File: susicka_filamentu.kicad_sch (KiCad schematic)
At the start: 33 parts, among them J1 USB_C_Receptacle_USB2.0_16P, J2 Conn_01x03, J3 Conn_01x04, J5 SHT40_I2C, J6 HX711_Weight, J7 Heater_Output, Q1 AO3400A, U1 RP2350A-QFN60

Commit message: revert(pcb): restore original clean schematic file to prevent KiCad crash
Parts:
- removed J5: SHT40_I2C, Connector_PinHeader_2.54mm:PinHeader_1x04_P2.54mm_Vertical, symbol Connector_Generic:Conn_01x04
- removed J6: HX711_Weight, Connector_PinHeader_2.54mm:PinHeader_1x04_P2.54mm_Vertical, symbol Connector_Generic:Conn_01x04
- removed J7: Heater_Output, TerminalBlock_Phoenix:TerminalBlock_Phoenix_MKDS-1,5-2_1x02_P5.00mm_Horizontal, symbol Connector_Generic:Conn_01x02
- removed Q1: AO3400A, Package_TO_SOT_SMD:SOT-23, symbol Transistor_FET:Q_NMOS_GSD
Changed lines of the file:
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@@
 		)
 	)
-		(symbol
-		(lib_id "Connector_Generic:Conn_01x04")
-		(at 180.34 165.1 0)
-		(unit 1)
-		(exclude_from_sim no)
-		(in_bom yes)
-		(on_board yes)
-		(dnp no)
-		(fields_autoplaced yes)
-		(property "Reference" "J5"
-			(at 180.34 156.21 0)
-			(effects (font (size 1.27 1.27)))
-		)
-		(property "Value" "SHT40_I2C"
-			(at 180.34 158.75 0)
-			(effects (font (size 1.27 1.27)))
-		)
-		(property "Footprint" "Connector_PinHeader_2.54mm:PinHeader_1x04_P2.54mm_Vertical"
-			(at 180.34 165.1 0)
-			(effects (font (size 1.27 1.27)) (hide yes))
-		)
-		(property "Datasheet" "~"
-			(at 180.34 165.1 0)
-			(effects (font (size 1.27 1.27)) (hide yes))
-		)
-		(property "Description" "Generic connector 1x04 for SHT40 Temp/Humidity Sensor"
-			(at 180.34 165.1 0)
-			(effects (font (size 1.27 1.27)) (hide yes))
-		)
-		(pin "1")
-		(pin "2")
-		(pin "3")
-		(pin "4")
-		(instances
-			(project ""
-				(path "/202a5452-a4a8-46b1-91e1-aa7f241e9adc"
-					(reference "J5")
-					(unit 1)
-				)
-			)
-		)
-	)
-	(symbol
-		(lib_id "Connector_Generic:Conn_01x04")
-		(at 210.82 165.1 0)
-		(unit 1)
-		(exclude_from_sim no)
-		(in_bom yes)
-		(on_board yes)
-		(dnp no)
-		(fields_autoplaced yes)
-		(property "Reference" "J6"
-			(at 210.82 156.21 0)
-			(effects (font (size 1.27 1.27)))
-		)
-		(property "Value" "HX711_Weight"
-			(at 210.82 158.75 0)
-			(effects (font (size 1.27 1.27)))
-		)
-		(property "Footprint" "Connector_PinHeader_2.54mm:PinHeader_1x04_P2.54mm_Vertical"
-			(at 210.82 165.1 0)
-			(effects (font (size 1.27 1.27)) (hide yes))
-		)
-		(property "Datasheet" "~"
-			(at 210.82 165.1 0)
-			(effects (font (size 1.27 1.27)) (hide yes))
-		)
-		(property "Description" "Generic connector 1x04 for HX711 Load Cell Amplifier"
-			(at 210.82 165.1 0)
-			(effects (font (size 1.27 1.27)) (hide yes))
-		)
-		(pin "1")
-		(pin "2")
-		(pin "3")
-		(pin "4")
-		(instances
-			(project ""
-				(path "/202a5452-a4a8-46b1-91e1-aa7f241e9adc"
-					(reference "J6")
-					(unit 1)
-				)
-			)
-		)
-	)
-	(symbol
-		(lib_id "Transistor_FET:Q_NMOS_GSD")
-		(at 245.11 165.1 0)
-		(unit 1)
-		(exclude_from_sim no)
-		(in_bom yes)
-		(on_board yes)
-		(dnp no)
-		(fields_autoplaced yes)
-		(property "Reference" "Q1"
-			(at 245.11 156.21 0)
-			(effects (font (size 1.27 1.27)))
-		)
-		(property "Value" "AO3400A"
-			(at 245.11 158.75 0)
-			(effects (font (size 1.27 1.27)))
-		)
-		(property "Footprint" "Package_TO_SOT_SMD:SOT-23"
-			(at 245.11 165.1 0)
-			(effects (font (size 1.27 1.27)) (hide yes))
-		)
-		(property "Datasheet" "~"
-			(at 245.11 165.1 0)
-			(effects (font (size 1.27 1.27)) (hide yes))
-		)
-		(property "Description" "N-Channel MOSFET Heater Switch"
-			(at 245.11 165.1 0)
-			(effects (font (size 1.27 1.27)) (hide yes))
-		)
-		(pin "1")
-		(pin "2")
-		(pin "3")
-		(instances
-			(project ""
-				(path "/202a5452-a4a8-46b1-91e1-aa7f241e9adc"
-					(reference "Q1")
-					(unit 1)
-				)
-			)
-		)
-	)
-	(symbol
-		(lib_id "Connector_Generic:Conn_01x02")
-		(at 275.6 165.1 0)
-		(unit 1)
-		(exclude_from_sim no)
-		(in_bom yes)
-		(on_board yes)
-		(dnp no)
-		(fields_autoplaced yes)
-		(property "Reference" "J7"
-			(at 275.6 156.21 0)
-			(effects (font (size 1.27 1.27)))
-		)
-		(property "Value" "Heater_Output"
-			(at 275.6 158.75 0)
-			(effects (font (size 1.27 1.27)))
-		)
-		(property "Footprint" "TerminalBlock_Phoenix:TerminalBlock_Phoenix_MKDS-1,5-2_1x02_P5.00mm_Horizontal"
-			(at 275.6 165.1 0)
-			(effects (font (size 1.27 1.27)) (hide yes))
-		)
-		(property "Datasheet" "~"
-			(at 275.6 165.1 0)
-			(effects (font (size 1.27 1.27)) (hide yes))
-		)
-		(property "Description" "Heater Screw Terminal Output"
-			(at 275.6 165.1 0)
-			(effects (font (size 1.27 1.27)) (hide yes))
-		)
-		(pin "1")
-		(pin "2")
-		(instances
-			(project ""
-				(path "/202a5452-a4a8-46b1-91e1-aa7f241e9adc"
-					(reference "J7")
-					(unit 1)
-				)
-			)
-		)
-	)
-(sheet_instances
+	(sheet_instances
 		(path "/"
 			(page "1")

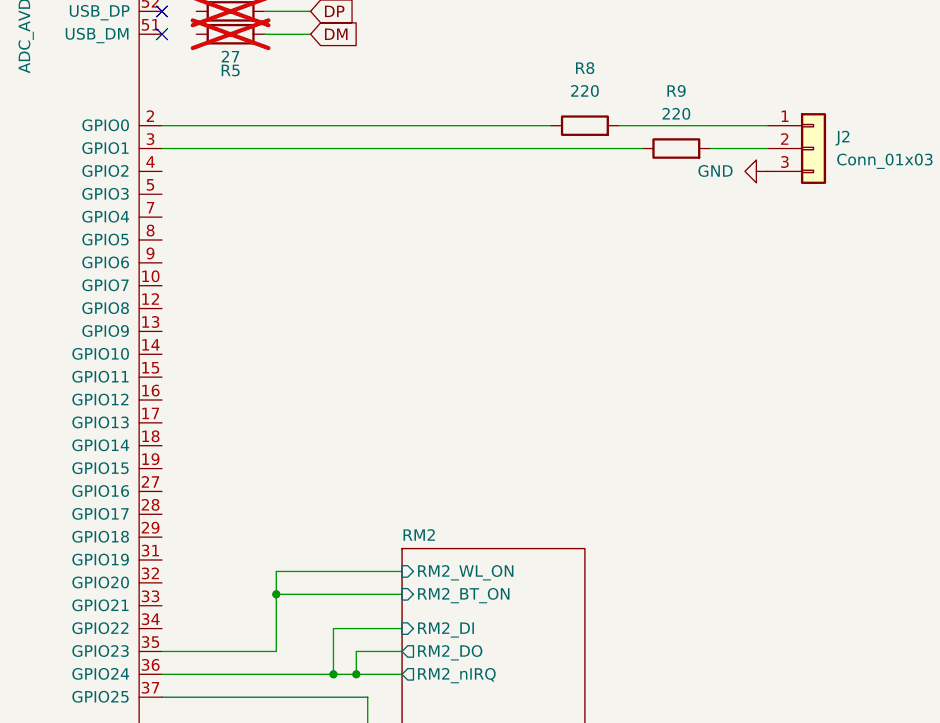
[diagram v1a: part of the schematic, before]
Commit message: feat(pcb): verify schematic components and assign KiCad 9 footprints for J5, J6, J7, Q1, R15, D2
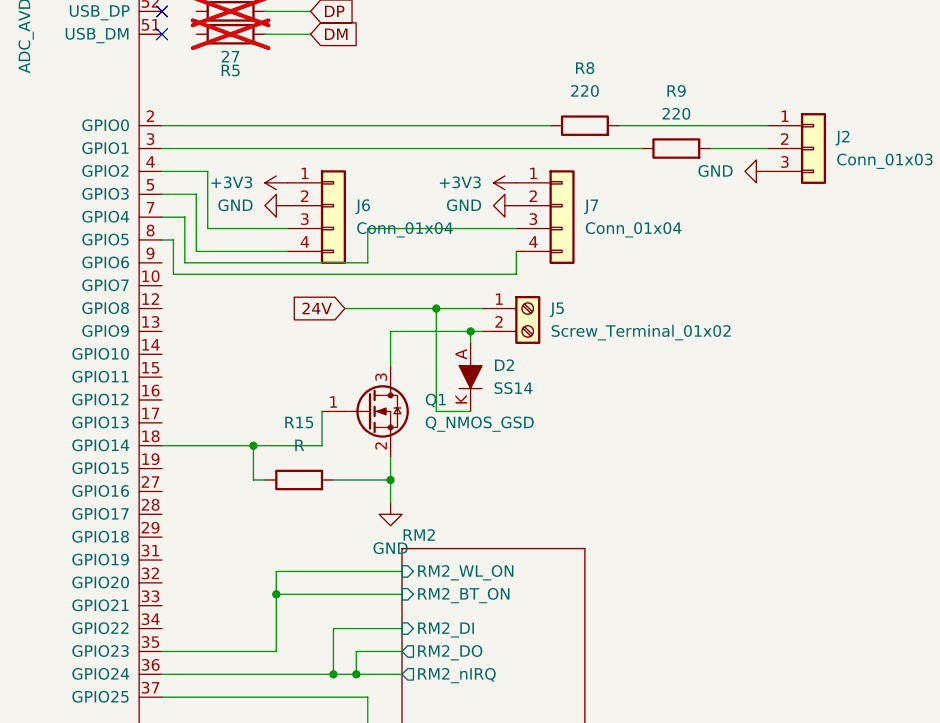
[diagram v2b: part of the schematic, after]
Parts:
- added D2: SS14, Diode_SMD:D_SMA, symbol dk_Diodes-Rectifiers-Single:SS14
- added J5: Screw_Terminal_01x02, TerminalBlock_Phoenix:TerminalBlock_Phoenix_MKDS-1,5-2_1x02_P5.00mm_Horizontal, symbol Connector:Screw_Terminal_01x02
- added J6, J7: Conn_01x04, Connector_PinHeader_2.54mm:PinHeader_1x04_P2.54mm_Vertical, symbol Connector_Generic:Conn_01x04
- added Q1: Q_NMOS_GSD, Package_TO_SOT_SMD:SOT-23, symbol Transistor_FET:Q_NMOS_GSD
- added R15: R, Resistor_SMD:R_0805_2012Metric, symbol Device:R
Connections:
- net +3V3: now also J6.1 (Pin_1), J7.1 (Pin_1)
- net GND: now also J6.2 (Pin_2), J7.2 (Pin_2), Q1.2 (S), R15.2
- net at U1.18 (GPIO14): now also Q1.1 (G), R15.1
- net at U1.4 (GPIO2): now also J6.3 (Pin_3)
- net at U1.5 (GPIO3): now also J6.4 (Pin_4)
- net at U1.7 (GPIO4): now also J7.3 (Pin_3)
- net at U1.8 (GPIO5): now also J7.4 (Pin_4)
- new net: D2.A, J5.2 (Pin_2), Q1.3 (D)
- new net 24V: D2.K, J5.1 (Pin_1)
